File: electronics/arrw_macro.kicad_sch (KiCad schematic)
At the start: 11 parts, among them SW59 SW_SPST, SW60 SW_SPST, SW61 SW_SPST, SW62 SW_SPST, SW63 SW_SPST, SW64 SW_SPST, SW65 SW_SPST, SW66 SW_SPST, SW67 SW_SPST, SW68 SW_SPST, U4 MAX7314AEG+

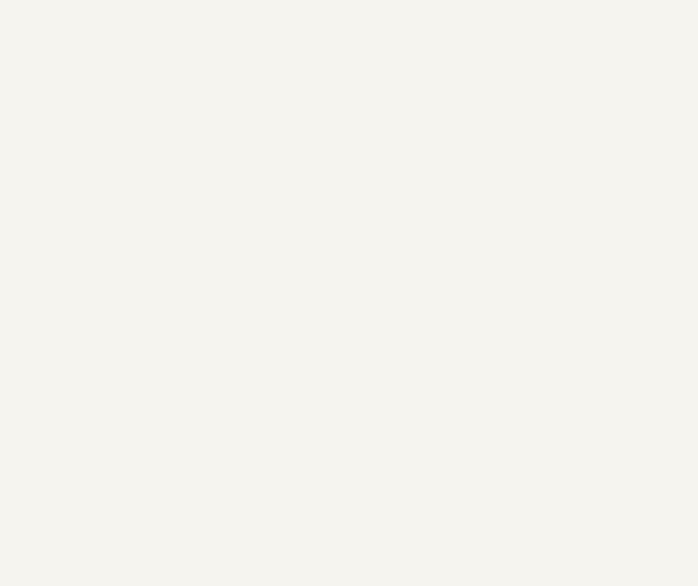
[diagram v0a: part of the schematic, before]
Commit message: add i2c headers to schematic
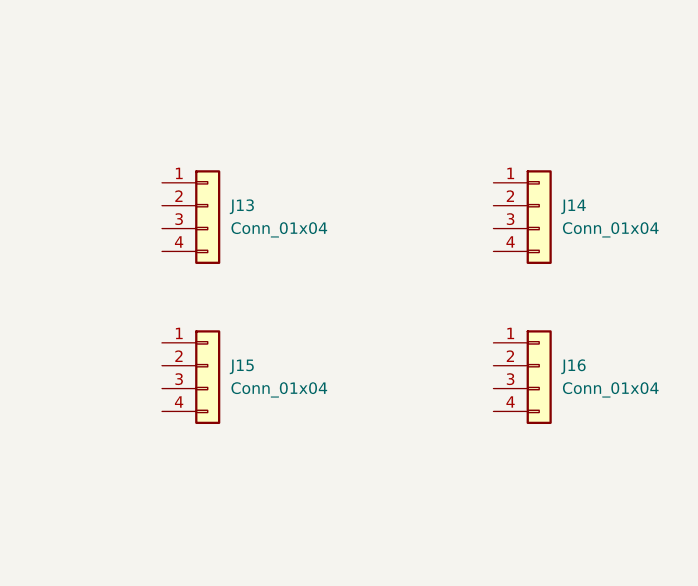
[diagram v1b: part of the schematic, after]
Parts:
- added J13, J14, J15, J16: Conn_01x04, symbol Connector_Generic:Conn_01x04
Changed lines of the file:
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@@
     (pin "2")
+  )
+  (symbol (lib_id "Connector_Generic:Conn_01x04") (at 210.82 81.28 0) (unit 1)
+    (in_bom yes) (on_board yes) (fields_autoplaced)
+    (property "Reference" "J16" (id 0) (at 213.36 81.2799 0)
+      (effects (font (size 1.27 1.27)) (justify left))
+    )
+    (property "Value" "Conn_01x04" (id 1) (at 213.36 83.8199 0)
+      (effects (font (size 1.27 1.27)) (justify left))
+    )
+    (property "Footprint" "" (id 2) (at 210.82 81.28 0)
+      (effects (font (size 1.27 1.27)) hide)
+    )
+    (property "Datasheet" "~" (id 3) (at 210.82 81.28 0)
+      (effects (font (size 1.27 1.27)) hide)
+    )
+    (pin "1")
+    (pin "2")
+    (pin "3")
+    (pin "4")
   )
   (symbol (lib_name "SW_SPST_4") (lib_id "Kailh:SW_SPST") (at 60.96 170.18 0) (unit 1)
@@
     (pin "1")
     (pin "2")
+  )
+  (symbol (lib_id "Connector_Generic:Conn_01x04") (at 173.99 63.5 0) (unit 1)
+    (in_bom yes) (on_board yes) (fields_autoplaced)
+    (property "Reference" "J13" (id 0) (at 176.53 63.4999 0)
+      (effects (font (size 1.27 1.27)) (justify left))
+    )
+    (property "Value" "Conn_01x04" (id 1) (at 176.53 66.0399 0)
+      (effects (font (size 1.27 1.27)) (justify left))
+    )
+    (property "Footprint" "" (id 2) (at 173.99 63.5 0)
+      (effects (font (size 1.27 1.27)) hide)
+    )
+    (property "Datasheet" "~" (id 3) (at 173.99 63.5 0)
+      (effects (font (size 1.27 1.27)) hide)
+    )
+    (pin "1")
+    (pin "2")
+    (pin "3")
+    (pin "4")
   )
   (symbol (lib_name "SW_SPST_5") (lib_id "Kailh:SW_SPST") (at 60.96 154.94 0) (unit 1)
@@
     (pin "2")
   )
+  (symbol (lib_id "Connector_Generic:Conn_01x04") (at 210.82 63.5 0) (unit 1)
+    (in_bom yes) (on_board yes) (fields_autoplaced)
+    (property "Reference" "J14" (id 0) (at 213.36 63.4999 0)
+      (effects (font (size 1.27 1.27)) (justify left))
+    )
+    (property "Value" "Conn_01x04" (id 1) (at 213.36 66.0399 0)
+      (effects (font (size 1.27 1.27)) (justify left))
+    )
+    (property "Footprint" "" (id 2) (at 210.82 63.5 0)
+      (effects (font (size 1.27 1.27)) hide)
+    )
+    (property "Datasheet" "~" (id 3) (at 210.82 63.5 0)
+      (effects (font (size 1.27 1.27)) hide)
+    )
+    (pin "1")
+    (pin "2")
+    (pin "3")
+    (pin "4")
+  )
+  (symbol (lib_id "Connector_Generic:Conn_01x04") (at 173.99 81.28 0) (unit 1)
+    (in_bom yes) (on_board yes) (fields_autoplaced)
+    (property "Reference" "J15" (id 0) (at 176.53 81.2799 0)
+      (effects (font (size 1.27 1.27)) (justify left))
+    )
+    (property "Value" "Conn_01x04" (id 1) (at 176.53 83.8199 0)
+      (effects (font (size 1.27 1.27)) (justify left))
+    )
+    (property "Footprint" "" (id 2) (at 173.99 81.28 0)
+      (effects (font (size 1.27 1.27)) hide)
+    )
+    (property "Datasheet" "~" (id 3) (at 173.99 81.28 0)
+      (effects (font (size 1.27 1.27)) hide)
+    )
+    (pin "1")
+    (pin "2")
+    (pin "3")
+    (pin "4")
+  )
   (symbol (lib_name "SW_SPST_6") (lib_id "Kailh:SW_SPST") (at 81.28 121.92 0) (unit 1)

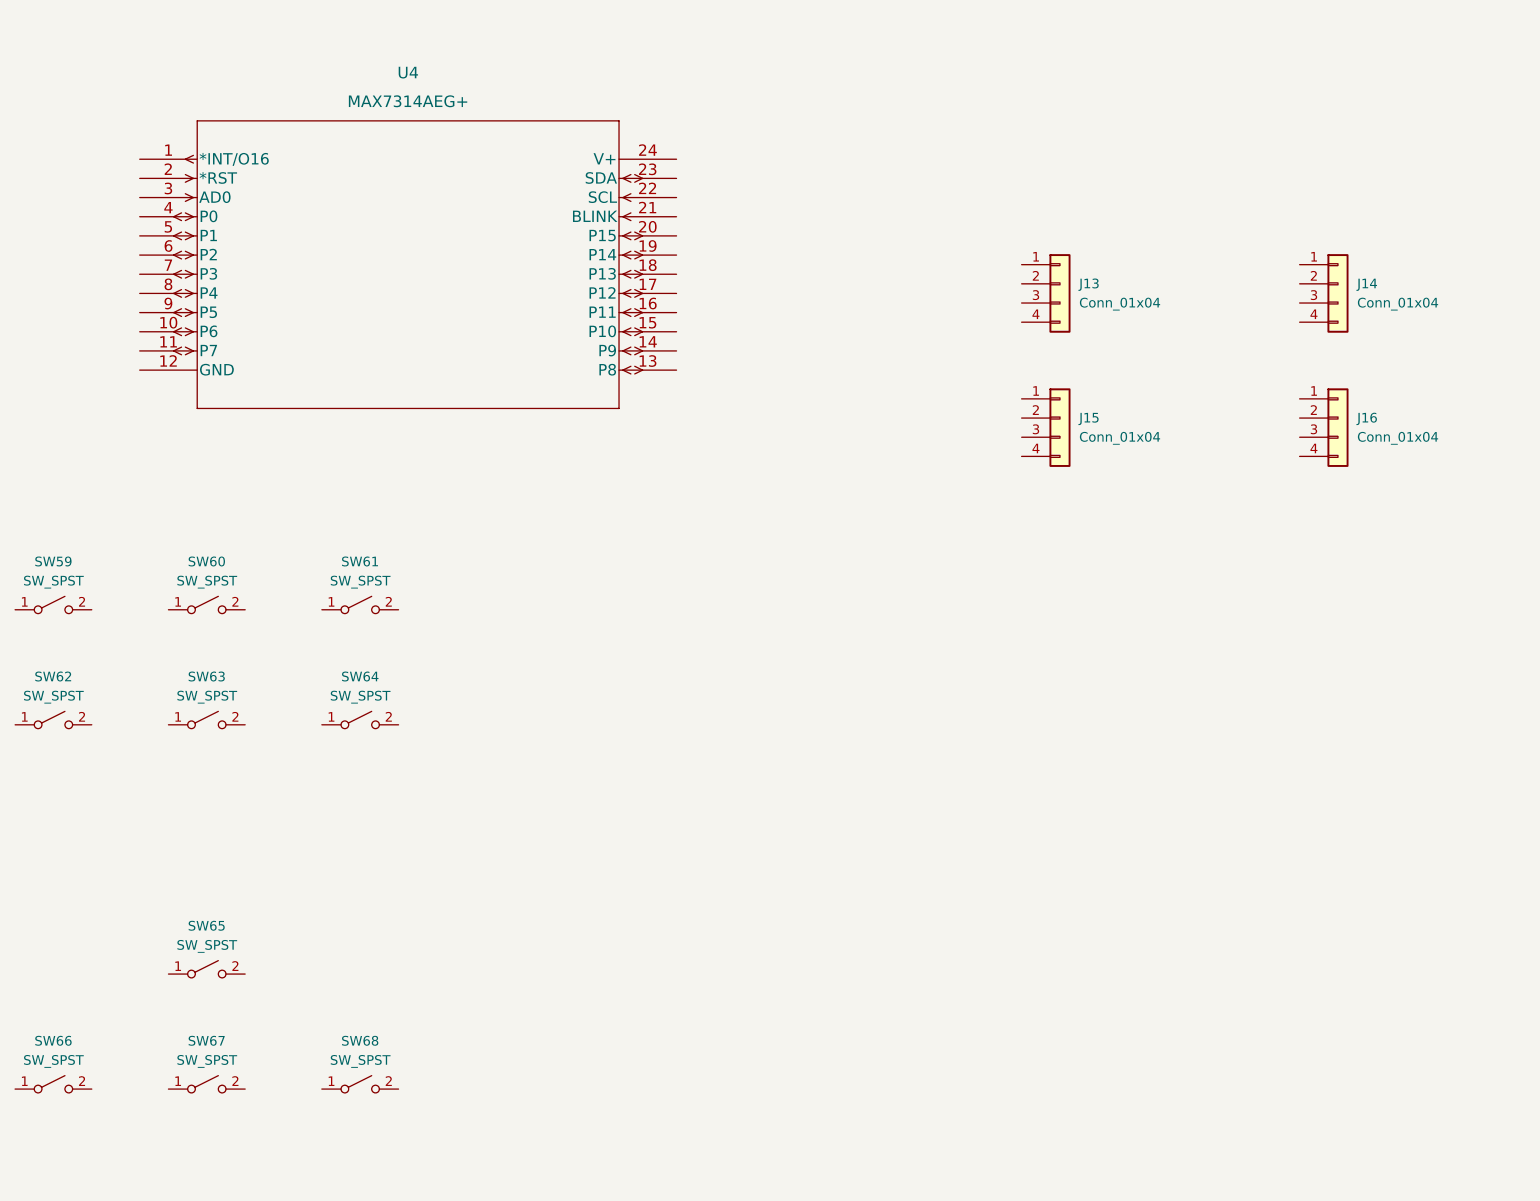
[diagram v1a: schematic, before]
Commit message: label switch nets
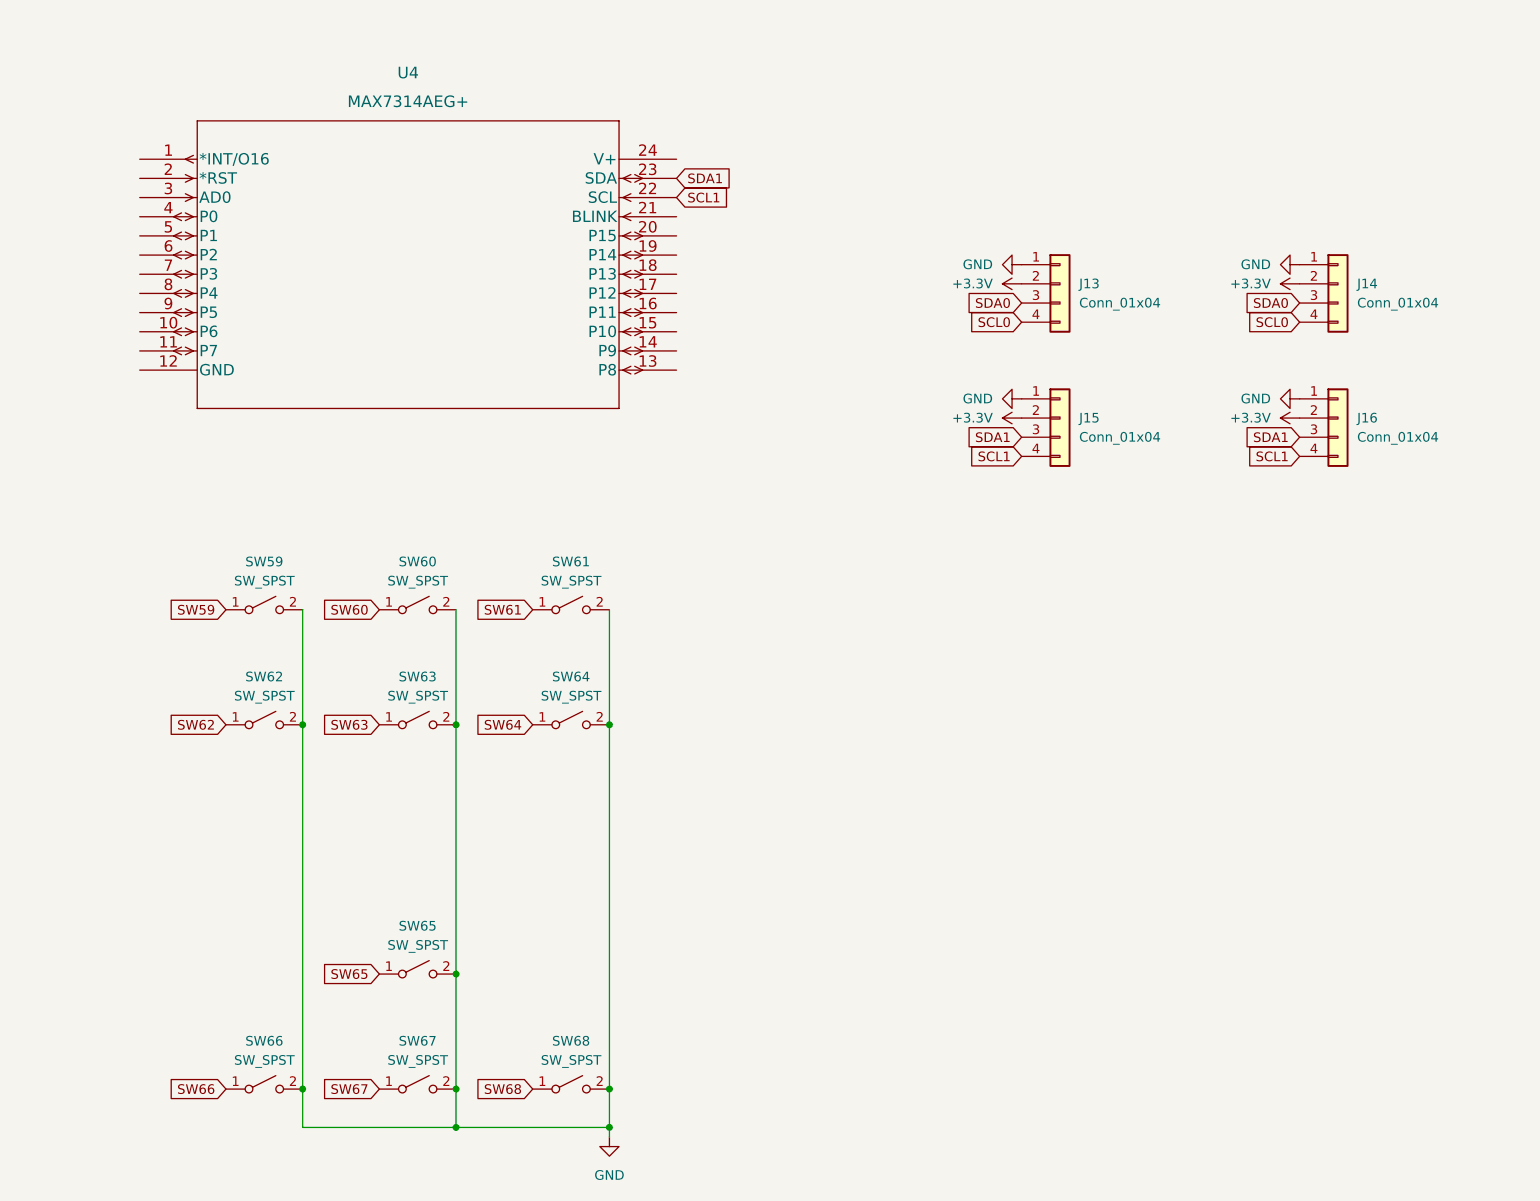
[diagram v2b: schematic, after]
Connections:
- net SW68: now reaches SW68.1 (A)
- net GND: now reaches SW68.2 (B)
- net GND: now also J13.1 (Pin_1), J14.1 (Pin_1), J15.1 (Pin_1), J16.1 (Pin_1), SW59.2 (B), SW60.2 (B), SW61.2 (B), SW62.2 (B), SW63.2 (B), SW64.2 (B), SW65.2 (B), SW66.2 (B), SW67.2 (B)
- net SW66: now reaches SW66.1 (A)
- net +3V3: now reaches J16.2 (Pin_2)
- net +3V3: now also J13.2 (Pin_2), J14.2 (Pin_2), J15.2 (Pin_2)
- net SDA1: now reaches J16.3 (Pin_3)
- net SDA1: now also J15.3 (Pin_3), U4.23 (SDA)
- net SCL1: now reaches J16.4 (Pin_4)
- net SCL1: now also J15.4 (Pin_4), U4.22 (SCL)
- net SW67: now reaches SW67.1 (A)
- net SW61: now reaches SW61.1 (A)
- net SDA0: now reaches J13.3 (Pin_3)
- net SDA0: now also J14.3 (Pin_3)
- net SCL0: now reaches J13.4 (Pin_4)
- net SCL0: now also J14.4 (Pin_4)
- net SW65: now reaches SW65.1 (A)
- net SW60: now reaches SW60.1 (A)
- net SW62: now reaches SW62.1 (A)
- net SW59: now reaches SW59.1 (A)
- net SW63: now reaches SW63.1 (A)
- net SW64: now reaches SW64.1 (A)
